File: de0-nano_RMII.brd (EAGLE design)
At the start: 72.5 x 49 mm, 34 parts, among them U1 DP83848, X1 1-227161-2

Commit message: almost done
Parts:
- removed X4: (no value), con-lstb:MA04-1
- added J1: (no value), con-jack:SPC4078
- added J2: (no value), seeed_connector:PW-3P-2.5
- added J3: (no value), seeed_connector:4P-65/35MIL
- moved X2 0.40 mm to (34.6, 2.60)
- moved X3 0.40 mm to (34.6, 46.4)
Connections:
- new net VCC_SYS: J3.1, J3.2
- net GND: now also J1.1, J1.2, J3.3, J3.4
- net OSCIN: now also X2.17
- net RXD_0: now also X2.33
- net RXD_1: now also X2.34
- net TXD_0: now also X2.39
- net TXD_1: now also X2.40
- net TX_EN: now also X2.37
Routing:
- net TXD_1: track 38.9 -> 48.3 mm
- net OSCIN: track 0.00 -> 8.33 mm
- net RXD_1: track 29.9 -> 36.0 mm
- net TXD_0: track 36.9 -> 42.1 mm
- net TX_EN: track 35.1 -> 39.0 mm
- net RXD_0: track 29.1 -> 31.7 mm
- net 3V3: track 53.0 -> 53.9 mm

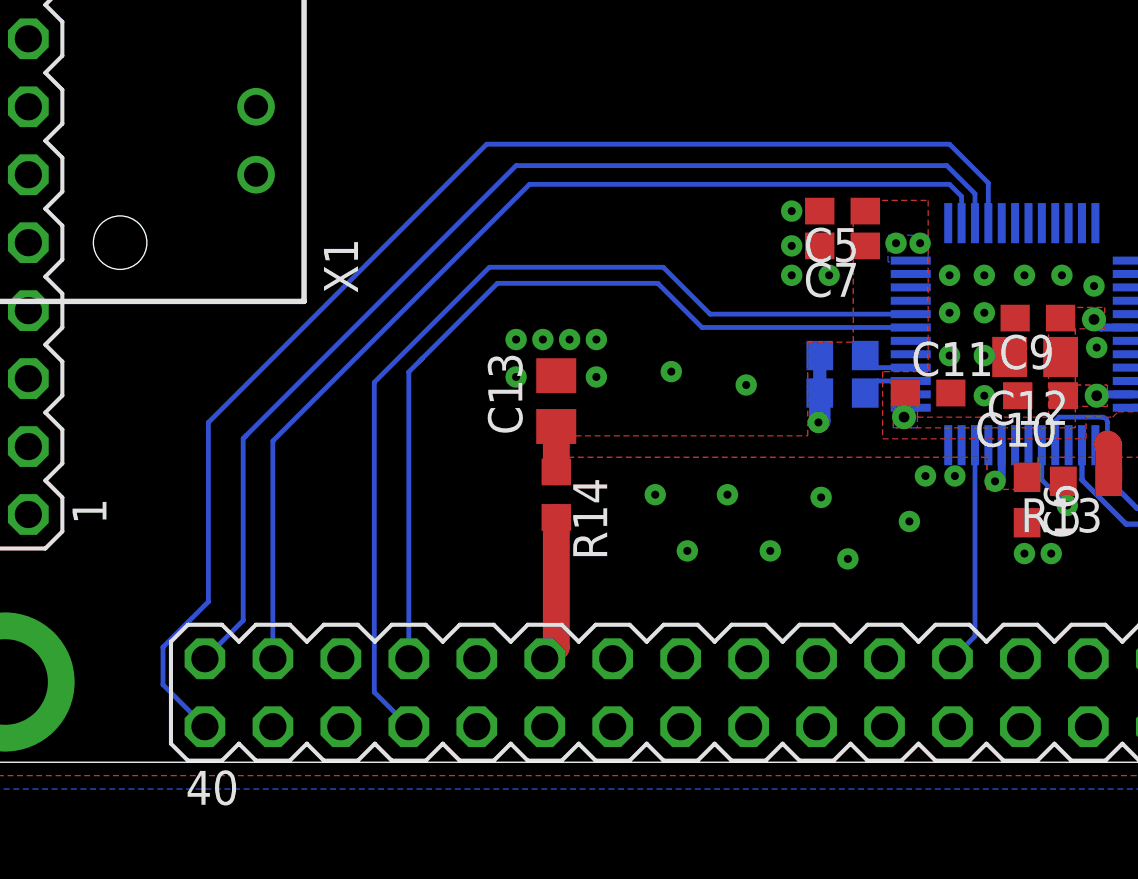
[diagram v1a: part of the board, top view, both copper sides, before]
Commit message: RX_DV and CRS_DV added
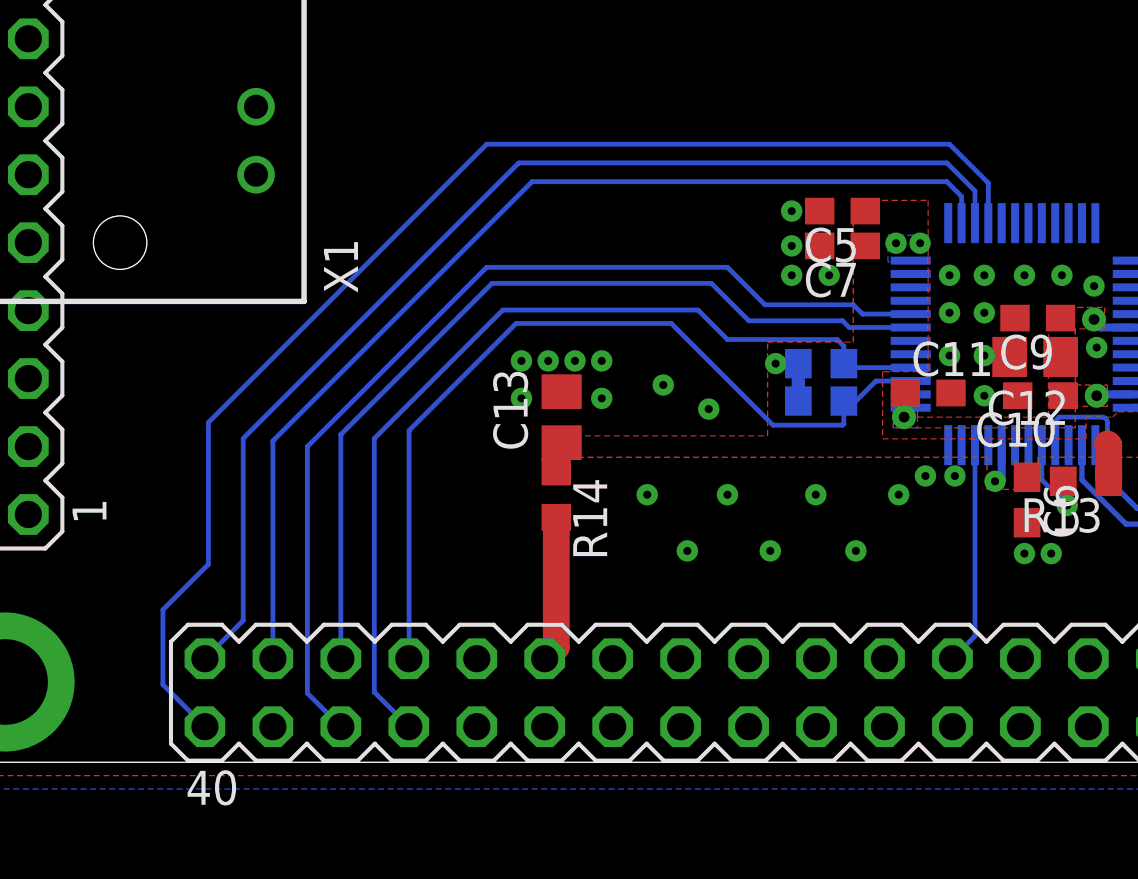
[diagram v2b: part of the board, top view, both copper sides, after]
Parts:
- moved R3 0.85 mm to (33.5, 13.5)
- moved R4 0.85 mm to (33.5, 14.9)
- moved C13 0.63 mm to (23.8, 12.9)
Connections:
- removed net N$1: R3.1, U1.39
- removed net N$2: R4.1, U1.40
- new net CRS_DV: R4.1, U1.40, X2.34
- new net RX_DV: R3.1, U1.39, X2.33
- net RXD_0: now also X2.35; no longer X2.33
- net RXD_1: now also X2.36; no longer X2.34
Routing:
- net CRS_DV: track 0.00 -> 34.8 mm
- net RX_DV: track 0.00 -> 31.7 mm
- net N$2: track 1.92 -> 0.00 mm
- net N$1: track 1.89 -> 0.00 mm
- net RXD_1: track 36.0 -> 37.0 mm
- net RXD_0: track 31.7 -> 32.7 mm
- net 3V3: track 53.9 -> 53.1 mm

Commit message: test branch
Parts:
- added C14: 10uF, resistor:C0805
- added C15: 100nF, resistor:C0603
- added IC1: (no value), linear-technology:TSOT23-6
- added R15: BLM, resistor:R0603
- moved J2 3.81 mm to (47.8, 30.5)
- moved J1 0.94 mm to (63.7, 35.3)
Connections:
- new net 3V3_A: C14.1, C15.1, IC1.4, R15.1
- new net N$1: R15.2, X3.29
- net GND: now also C14.2, C15.2, IC1.2, IC1.6
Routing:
- net 3V3_A: track 0.00 -> 31.3 mm
- net N$1: track 0.00 -> 3.41 mm
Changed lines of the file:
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@@
 <?xml version="1.0" encoding="utf-8"?>
 <!DOCTYPE eagle SYSTEM "eagle.dtd">
-<eagle version="8.0.2">
+<eagle version="7.6.0">
 <drawing>
 <settings>
@@
 <element name="R14" library="resistor" package="R0603" value="BLM" x="23.6" y="10" rot="R270"/>
 <element name="C13" library="resistor" package="C0805" value="10uF" x="23.8" y="12.9" rot="R90"/>
-<element name="J1" library="con-jack" package="SPC4078" value="" x="64.5" y="35.8" rot="R180">
-<attribute name="MF" value="" x="64.5" y="35.8" size="1.778" layer="27" rot="R180" display="off"/>
-<attribute name="MPN" value="" x="64.5" y="35.8" size="1.778" layer="27" rot="R180" display="off"/>
-<attribute name="OC_FARNELL" value="unknown" x="64.5" y="35.8" size="1.778" layer="27" rot="R180" display="off"/>
-<attribute name="OC_NEWARK" value="unknown" x="64.5" y="35.8" size="1.778" layer="27" rot="R180" display="off"/>
+<element name="J1" library="con-jack" package="SPC4078" value="" x="63.7" y="35.3" rot="R180">
+<attribute name="MF" value="" x="63.7" y="35.3" size="1.778" layer="27" rot="R180" display="off"/>
+<attribute name="MPN" value="" x="63.7" y="35.3" size="1.778" layer="27" rot="R180" display="off"/>
+<attribute name="OC_FARNELL" value="unknown" x="63.7" y="35.3" size="1.778" layer="27" rot="R180" display="off"/>
+<attribute name="OC_NEWARK" value="unknown" x="63.7" y="35.3" size="1.778" layer="27" rot="R180" display="off"/>
 </element>
-<element name="J2" library="seeed_connector" package="PW-3P-2.5" value="" x="48" y="34.3" rot="R180"/>
+<element name="J2" library="seeed_connector" package="PW-3P-2.5" value="" x="47.8" y="30.5" rot="R180"/>
 <element name="J3" library="seeed_connector" package="4P-65/35MIL" value="" x="71.25" y="30.4"/>
+<element name="IC1" library="linear-technology" package="TSOT23-6" value="" x="21.1" y="26.3" rot="R270"/>
+<element name="R15" library="resistor" package="R0603" value="BLM" x="46" y="40.9" rot="R90"/>
+<element name="C14" library="resistor" package="C0805" value="10uF" x="43.8" y="41" rot="R90"/>
+<element name="C15" library="resistor" package="C0603" value="100nF" x="25.1" y="26.3" rot="R90"/>
 </elements>
 <signals>
@@
 <contactref element="J1" pad="2"/>
 <contactref element="J1" pad="1"/>
+<contactref element="IC1" pad="2"/>
+<contactref element="IC1" pad="6"/>
+<contactref element="C14" pad="2"/>
+<contactref element="C15" pad="2"/>
+<via x="26.4" y="27" extent="1-16" drill="0.3" diameter="0.8"/>
+<via x="25.1" y="28.3" extent="1-16" drill="0.3" diameter="0.8"/>
+<via x="26.4" y="28.3" extent="1-16" drill="0.3" diameter="0.8"/>
+<via x="42.3" y="41.7" extent="1-16" drill="0.3" diameter="0.8"/>
+<via x="43.8" y="43.2" extent="1-16" drill="0.3" diameter="0.8"/>
+<via x="42.3" y="43.2" extent="1-16" drill="0.3" diameter="0.8"/>
 </signal>
 <signal name="OSCIN">
@@
 <wire x1="71.25" y1="31.67" x2="71.25" y2="34.21" width="0" layer="19" extent="1-1"/>
 </signal>
+<signal name="3V3_A">
+<contactref element="IC1" pad="4"/>
+<contactref element="C14" pad="1"/>
+<contactref element="R15" pad="1"/>
+<wire x1="46" y1="40.05" x2="43.8" y2="40.05" width="1" layer="1"/>
+<wire x1="26.75" y1="25.35" x2="41.4" y2="40" width="1" layer="1"/>
+<wire x1="41.4" y1="40" x2="43.75" y2="40" width="1" layer="1"/>
+<wire x1="43.75" y1="40" x2="43.8" y2="40.05" width="0.6" layer="1"/>
+<wire x1="26.75" y1="25.35" x2="23.45" y2="25.35" width="1" layer="1"/>
+<wire x1="22.4" y1="25.35" x2="23.45" y2="25.35" width="0.6" layer="1"/>
+<contactref element="C15" pad="1"/>
+<wire x1="26.75" y1="25.35" x2="25.6" y2="25.35" width="0.6" layer="1"/>
+<wire x1="25.6" y1="25.35" x2="25.1" y2="25.45" width="0.6" layer="1"/>
+</signal>
+<signal name="N$1">
+<contactref element="R15" pad="2"/>
+<contactref element="X3" pad="29"/>
+<wire x1="46.03" y1="45.13" x2="46" y2="45.13" width="1" layer="1"/>
+<wire x1="46" y1="45.13" x2="46" y2="41.75" width="1" layer="1"/>
+</signal>
 </signals>

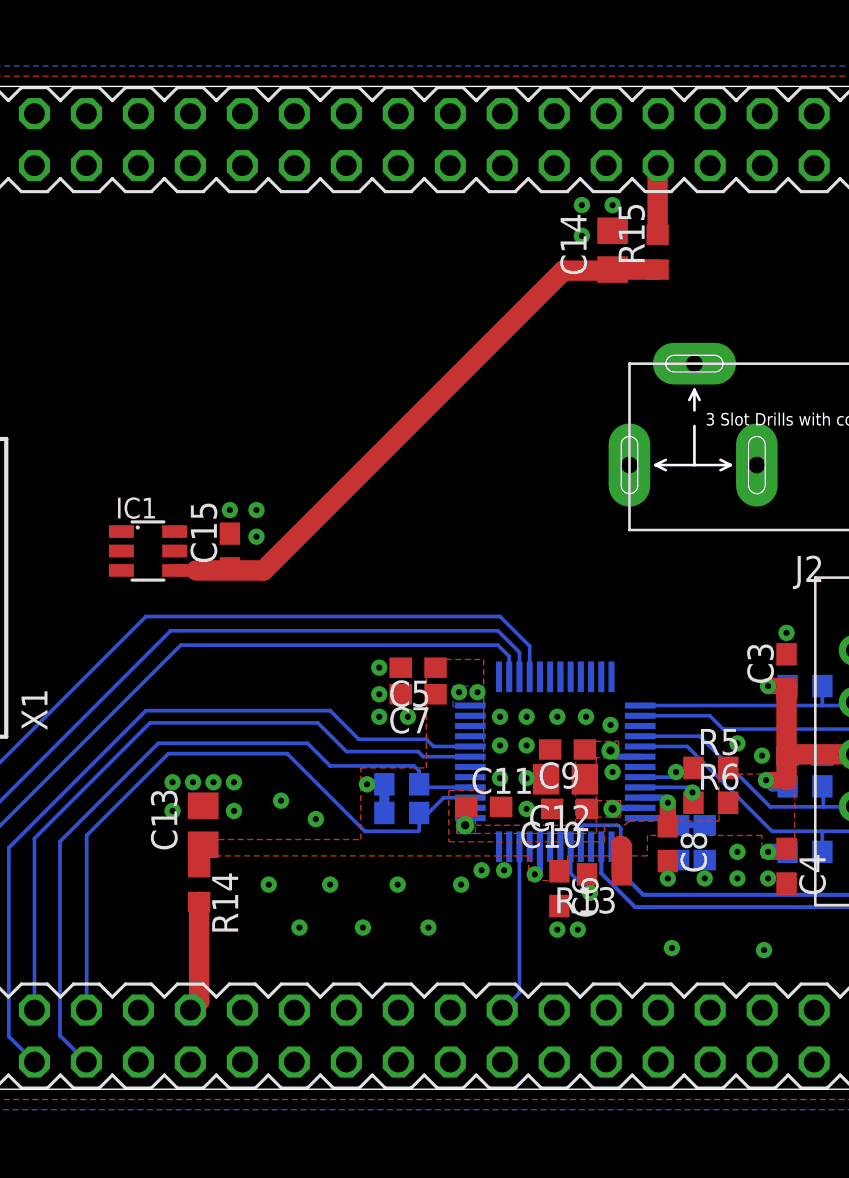
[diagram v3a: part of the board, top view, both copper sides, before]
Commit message: removed some pads on connector
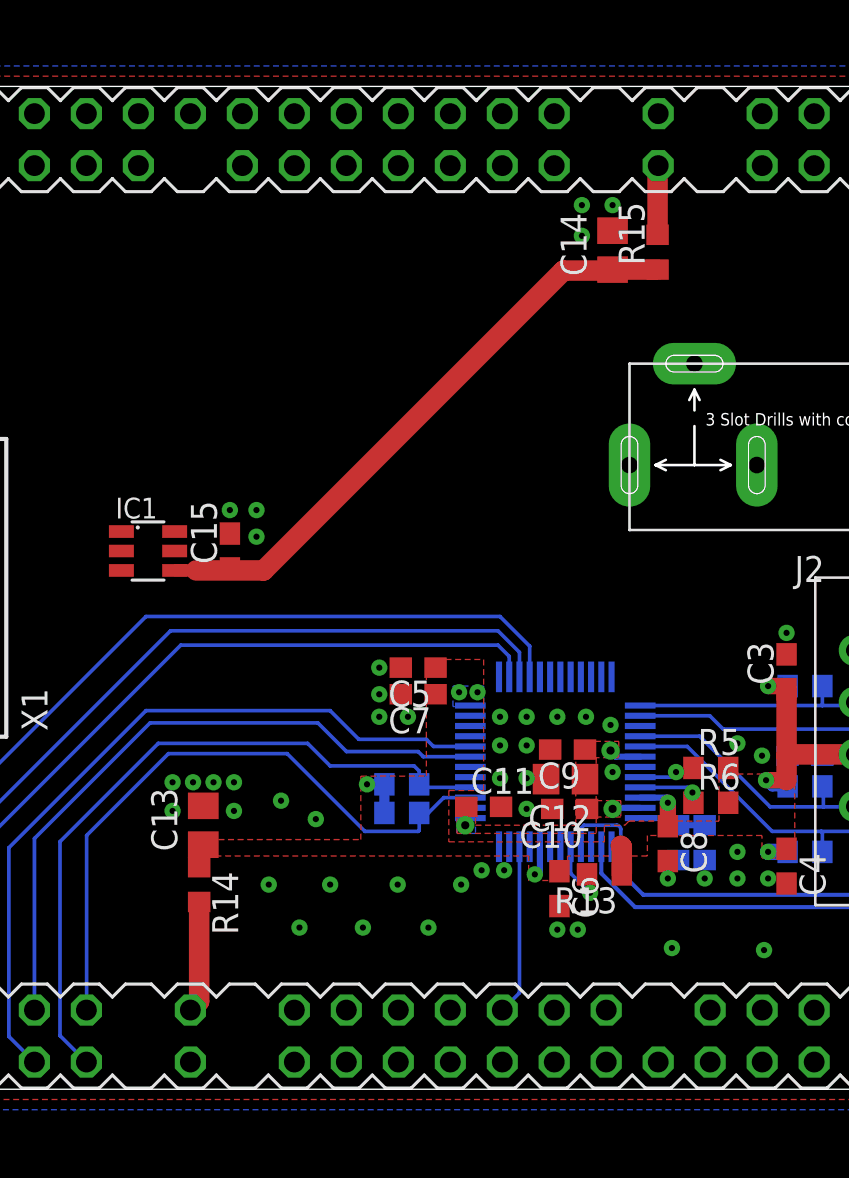
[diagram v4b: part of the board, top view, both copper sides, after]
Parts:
- X2, X3: device con-lstb:MA20-2 -> con-lstb:MA20-2_ALT
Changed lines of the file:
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@@
 <?xml version="1.0" encoding="utf-8"?>
 <!DOCTYPE eagle SYSTEM "eagle.dtd">
-<eagle version="7.6.0">
+<eagle version="8.0.2">
 <drawing>
 <settings>
@@
 <attribute name="OC_NEWARK" value="unknown" x="2.6" y="24.5" size="1.778" layer="27" rot="R90" display="off"/>
 </element>
-<element name="X2" library="con-lstb" package="MA20-2" value="" x="34.6" y="2.6" rot="R180">
-<attribute name="MF" value="" x="34.6" y="2.6" size="1.778" layer="27" rot="R180" display="off"/>
-<attribute name="MPN" value="" x="34.6" y="2.6" size="1.778" layer="27" rot="R180" display="off"/>
-<attribute name="OC_FARNELL" value="unknown" x="34.6" y="2.6" size="1.778" layer="27" rot="R180" display="off"/>
-<attribute name="OC_NEWARK" value="unknown" x="34.6" y="2.6" size="1.778" layer="27" rot="R180" display="off"/>
-</element>
-<element name="X3" library="con-lstb" package="MA20-2" value="" x="34.6" y="46.4">
-<attribute name="MF" value="" x="34.6" y="46.4" size="1.778" layer="27" display="off"/>
-<attribute name="MPN" value="" x="34.6" y="46.4" size="1.778" layer="27" display="off"/>
-<attribute name="OC_FARNELL" value="unknown" x="34.6" y="46.4" size="1.778" layer="27" display="off"/>
-<attribute name="OC_NEWARK" value="unknown" x="34.6" y="46.4" size="1.778" layer="27" display="off"/>
-</element>
+<element name="X2" library="con-lstb" package="MA20-2_ALT" value="" x="34.6" y="2.6" rot="R180"/>
+<element name="X3" library="con-lstb" package="MA20-2_ALT" value="" x="34.6" y="46.4"/>
 <element name="X7" library="seeed_connector" package="RJ45" value="" x="64.5" y="17"/>
 <element name="U1" library="national-semiconductor" package="LQFP48" value="DP83848" x="41" y="16" rot="MR270">
@@
 <vertex x="23.6" y="12.2"/>
 <vertex x="31.5" y="12.2"/>
-<vertex x="31.5" y="15.7"/>
-<vertex x="34.7" y="15.7"/>
+<vertex x="31.5" y="15.3"/>
+<vertex x="34.7" y="15.3"/>
 <vertex x="34.7" y="21"/>
 <vertex x="37.5" y="21"/>

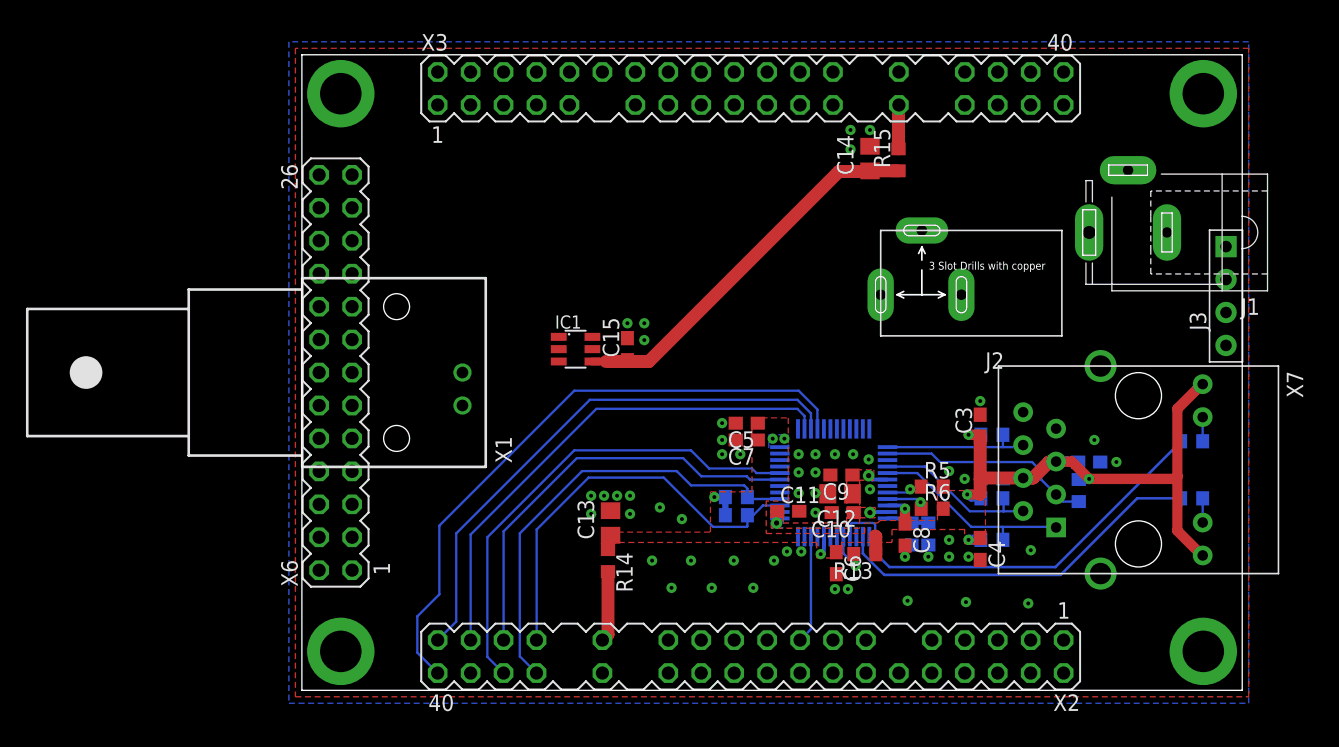
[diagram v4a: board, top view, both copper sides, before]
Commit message: added external power and DAC
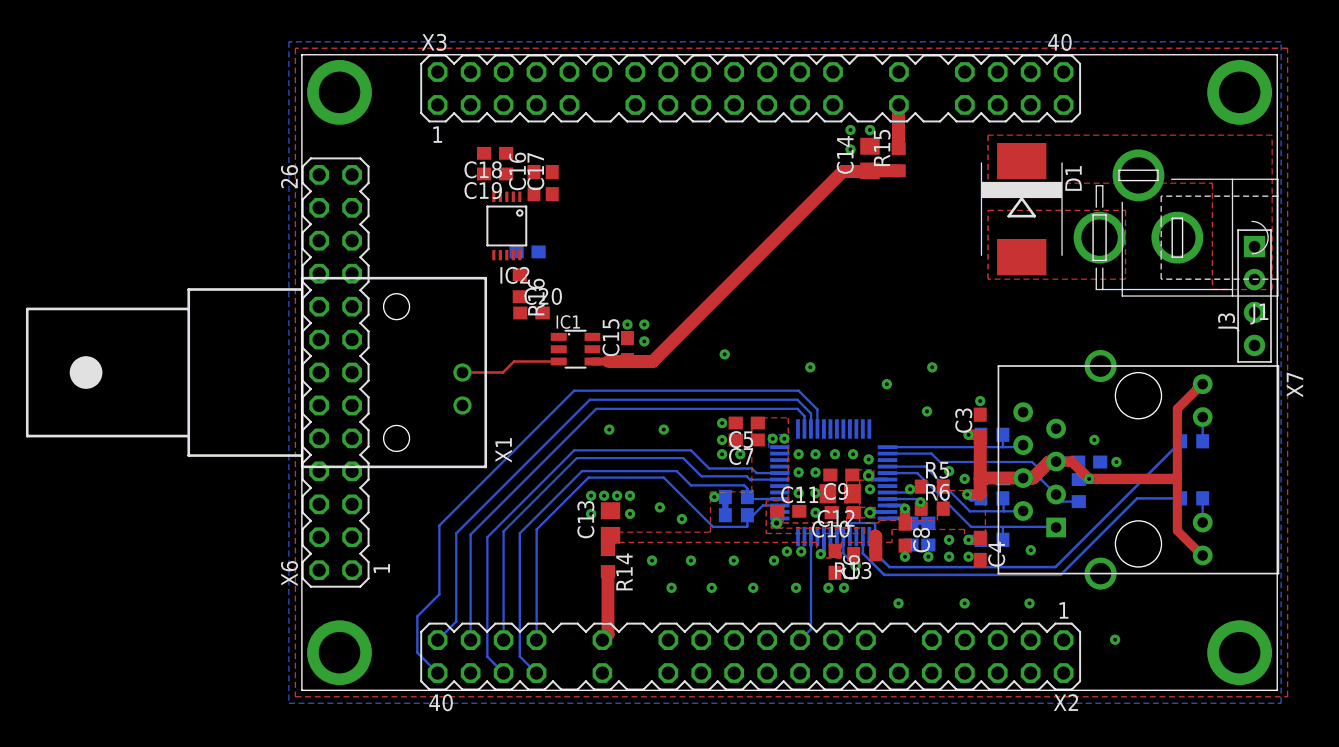
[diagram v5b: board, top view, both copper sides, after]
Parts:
- removed J2: (no value), seeed_connector:PW-3P-2.5
- added C16, C17, C18, C19, C20, C21: 100nF, resistor:C0603
- added D1: (no value), diode:SMC
- added IC2: AD5683, analog-devices:SO10
- added R16: 51R, resistor:R0603
- moved J3 2.20 mm to (73.5, 30.4)
- moved J1 0.89 mm to (64.5, 34.9)
- moved C6 0.14 mm to (41.1, 9.90)
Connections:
- new net COM_OUT: IC1.5
- new net N$10: IC2.8
- new net N$11: IC2.7
- new net N$12: IC2.6
- new net N$13: C21.1, IC2.9
- new net N$2: C18.1, C19.1, IC2.2, IC2.3
- new net N$8: IC2.10, R16.1
- new net THR_LVL: C20.1, IC1.1, R16.2
- new net V_RAW: D1.A, J1.3
- net 3V3_A: now also C16.1, C17.1, IC2.1
- net GND: now also C16.2, C17.2, C18.2, C19.2, C20.2, C21.2, IC2.4, IC2.5
- net SIG_IN: now also IC1.3
- net VCC_SYS: now also D1.C
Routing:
- net SIG_IN: track 0.00 -> 7.77 mm
- net 3V3: track 53.1 -> 54.0 mm
- added copper zone on layer 1, net VCC_SYS
- added copper zone on layer 1, net V_RAW
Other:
- board size 72.5 x 49 mm -> 75.2 x 49 mm

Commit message: almost done
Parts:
- added R17: 4k7, resistor:R0603
- X6: device con-lstb:MA13-2 -> con-lstb:MA13-2_ALT
- moved C18 3.22 mm to (15.3, 38.2), flipped to the bottom, turned to 0 degrees
- moved C15 2.90 mm to (22.2, 26.3)
- moved IC1 2.90 mm to (18.2, 26.3)
- moved C19 2.83 mm to (15.3, 37.0), flipped to the bottom, turned to 0 degrees
- moved C20 1.77 mm to (18.2, 30.8), turned to 90 degrees
- moved R16 0.40 mm to (16.8, 30.8)
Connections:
- net N$2 renamed VLOGIC
- removed net N$10: IC2.8
- removed net N$11: IC2.7
- removed net N$12: IC2.6
- new net DAC_CLK: IC2.6, X3.5
- new net DAC_NCS: IC2.7, R17.2, X3.7
- new net DAC_SDI: IC2.8, X3.6
- net 3V3_A: now also R17.1
- net COM_OUT: now also X3.13
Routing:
- net 3V3_A: track 31.6 -> 58.0 mm, vias 0 -> 2
- net DAC_SDI: track 0.00 -> 23.0 mm
- net COM_OUT: track 0.00 -> 22.1 mm
- net DAC_NCS: track 0.00 -> 18.4 mm
- net DAC_CLK: track 0.00 -> 17.0 mm
- net THR_LVL: track 0.00 -> 4.54 mm
- net SIG_IN: track 7.77 -> 4.87 mm
- net VLOGIC: track 0.00 -> 2.12 mm, vias 0 -> 1
- net N$13: track 0.00 -> 1.99 mm, vias 0 -> 1
- net N$8: track 0.00 -> 1.90 mm
- added copper zone on layer 1, net 3V3_A
- added copper zone on layer 1, net VLOGIC
